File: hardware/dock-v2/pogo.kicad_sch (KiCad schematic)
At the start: 0 parts

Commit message: Dock v2: all parts placed on their sheets (not wired)
149 parts across POWER, USB_PORTS, MCU_A, MCU_B, BLE and POGO (A3), in
labelled groups, with references (sheet x 100), values, footprints, LCSC
numbers (hidden LCSC field) and a Note per part. Only unconnected-pin ERC
messages remain.

5 V buck values from TI's TPS54331 Table 7-1 (5 V design), moved to Basic
parts: 12k/2.2k feedback (5.16 V), 51k + 4.7nF + 47pF compensation, 10 nF
soft start, 3 x 22 uF out; recorded in docs/dock-v2-power-input.md.
New footprint dock_v2:CP_Radial_D6.3mm_P5.00mm for the hand-soldered 220 uF.

Co-Authored-By: Claude Opus 5.5 <noreply@anthropic.com>
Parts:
- added C601, C603: 1uF, Capacitor_SMD:C_0402_1005Metric, symbol Device:C
- added C602: 10uF, Capacitor_SMD:C_0805_2012Metric, symbol Device:C
- added J601: Pogo 6-pin, dock:Pogo-6, symbol Connector_Generic:Conn_01x06
- added Q601: 2N7002, Package_TO_SOT_SMD:SOT-23, symbol Transistor_FET:2N7002
- added R601, R602, R603: 1k, Resistor_SMD:R_0402_1005Metric, symbol Device:R
- added R604, R607: 10k, Resistor_SMD:R_0402_1005Metric, symbol Device:R
- added R605: 100k, Resistor_SMD:R_0402_1005Metric, symbol Device:R
- added R606: 6.8k, Resistor_SMD:R_0402_1005Metric, symbol Device:R
- added R608: 15k, Resistor_SMD:R_0402_1005Metric, symbol Device:R
- added U601: TPD4E1U06DBVR, Package_TO_SOT_SMD:SOT-23-6, symbol dock_v2_custom:TPD4E1U06DBV
- added U602: SY6280AAC, Package_TO_SOT_SMD:SOT-23-5, symbol dock_v2_custom:SY6280AAC
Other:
- note added: "Pogo 5 V switch (hardware DET enable)"
- note added: "Pogo connector (front edge)"

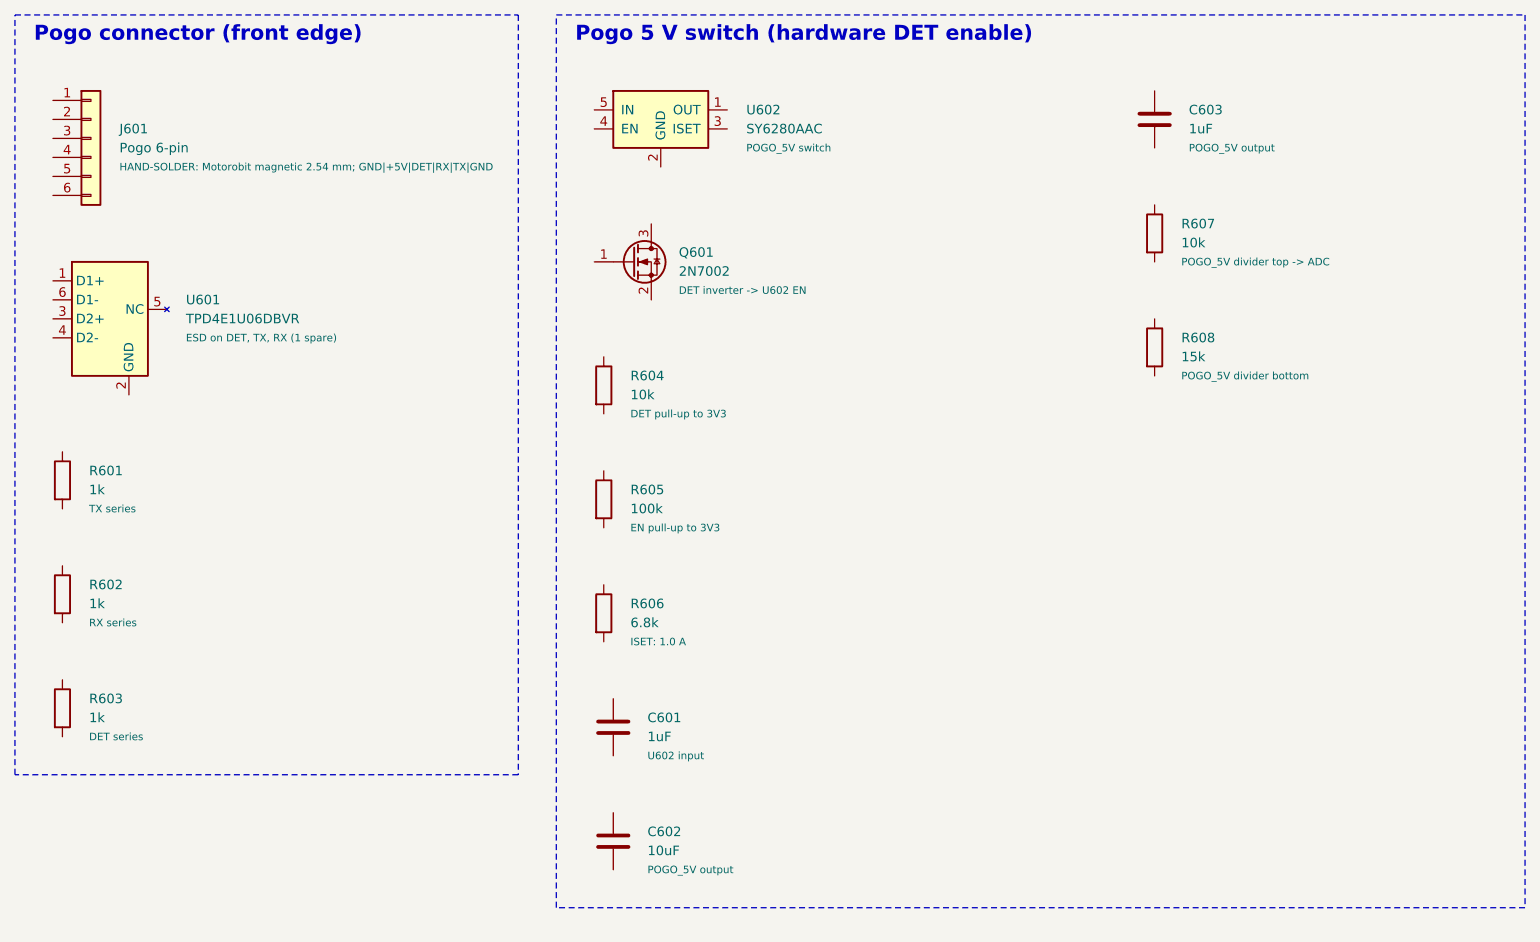
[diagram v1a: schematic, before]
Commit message: Dock v2: connection guide (DOCK_CONNECTIONS.md), pin maps, wiring checker
hardware/dock-v2/DOCK_CONNECTIONS.md, in the style of the pad's guide: per
sheet a sketch, parts table (value, footprint, LCSC, job), pin-by-pin wiring
tables, placement notes; MCU A/B pin maps; nets that cross sheets (global
labels); PWR_FLAG and no-connect lists; full net index. Tables are generated
from one connection model (tools/dock_v2_connections/dock_nets.py) that is
checked against the placed schematic: 570 pins, each on a net or NC exactly once.

Found while making the pin map: MCU A's pins are weak pull-downs at reset, so
added 10k pull-ups on B_RUN, B_BOOTSEL (R406, R407) and ESP32 GPIO9 (R504),
and POGO_OFF now drives its own 2N7002 (Q602, R609) so a blank MCU A can't
switch off pad charging. 154 parts.

tools/dock_v2_connections/check_wiring.py compares the wired schematic with
the guide (unwired / split / merged / NC); make_doc.py regenerates the guide.

Co-Authored-By: Claude Opus 5.5 <noreply@anthropic.com>
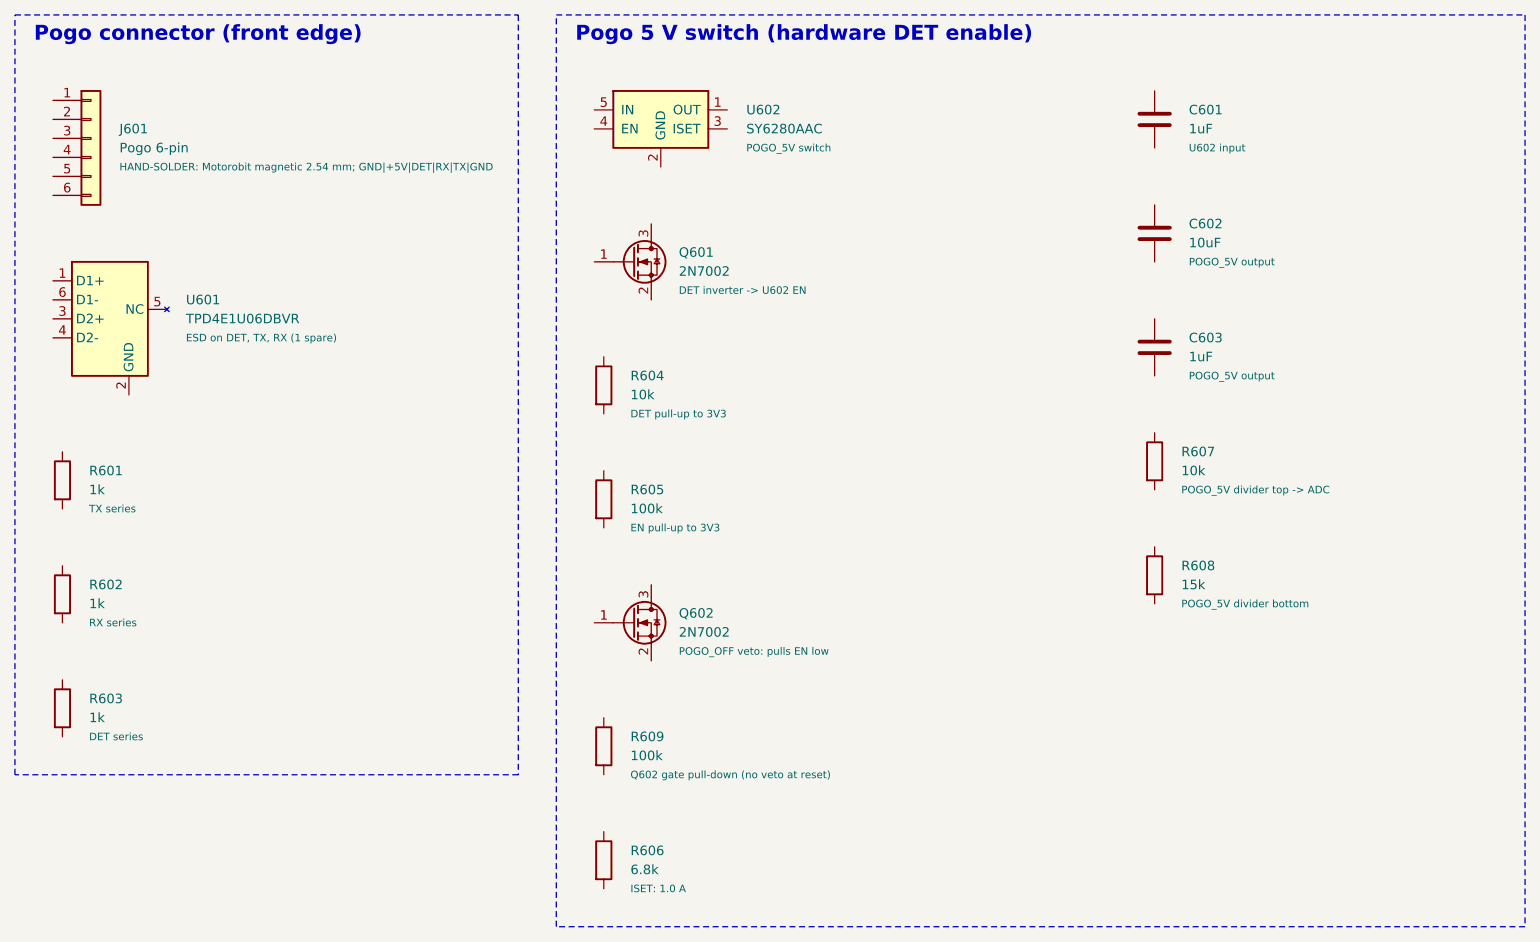
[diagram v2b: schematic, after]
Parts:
- added Q602: 2N7002, Package_TO_SOT_SMD:SOT-23, symbol Transistor_FET:2N7002
- added R609: 100k, Resistor_SMD:R_0402_1005Metric, symbol Device:R

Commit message: 7-pin pogo (2 x +5V, 2 x GND), README and DESIGN for the v2 dock
Pogo: both halves move from the 6-pin to the Motorobit 7-pin 2.54 mm magnetic
set (1 A per contact). Dock side GND | +5V | +5V | DET | RX | TX | GND, pad side
mirrored. New footprint dock:Pogo-7 (scaled from Pogo-6, marked through-hole).
Dock J601 -> Conn_01x07; pogo switch R606 6.8k -> 4.7k (1.45 A, 1.09-1.81 A,
below the 2 A of two contacts), so the pad no longer has to dim its LEDs while
docked. Pad pogo board J1 -> 7 pins, pins 5+6 = POGO_5V, pin 7 = GND (nets
verified before/after). Connection model, guide, pogo/power/placement docs and
PAD_CONNECTIONS updated.

README and DESIGN rewritten for the v2 dock (sections 1-7, 15-22); the pad
sections 8-14 are kept as the v1 plan, to be redesigned. v1 dock stays on master.

Co-Authored-By: Claude Opus 5.5 <noreply@anthropic.com>
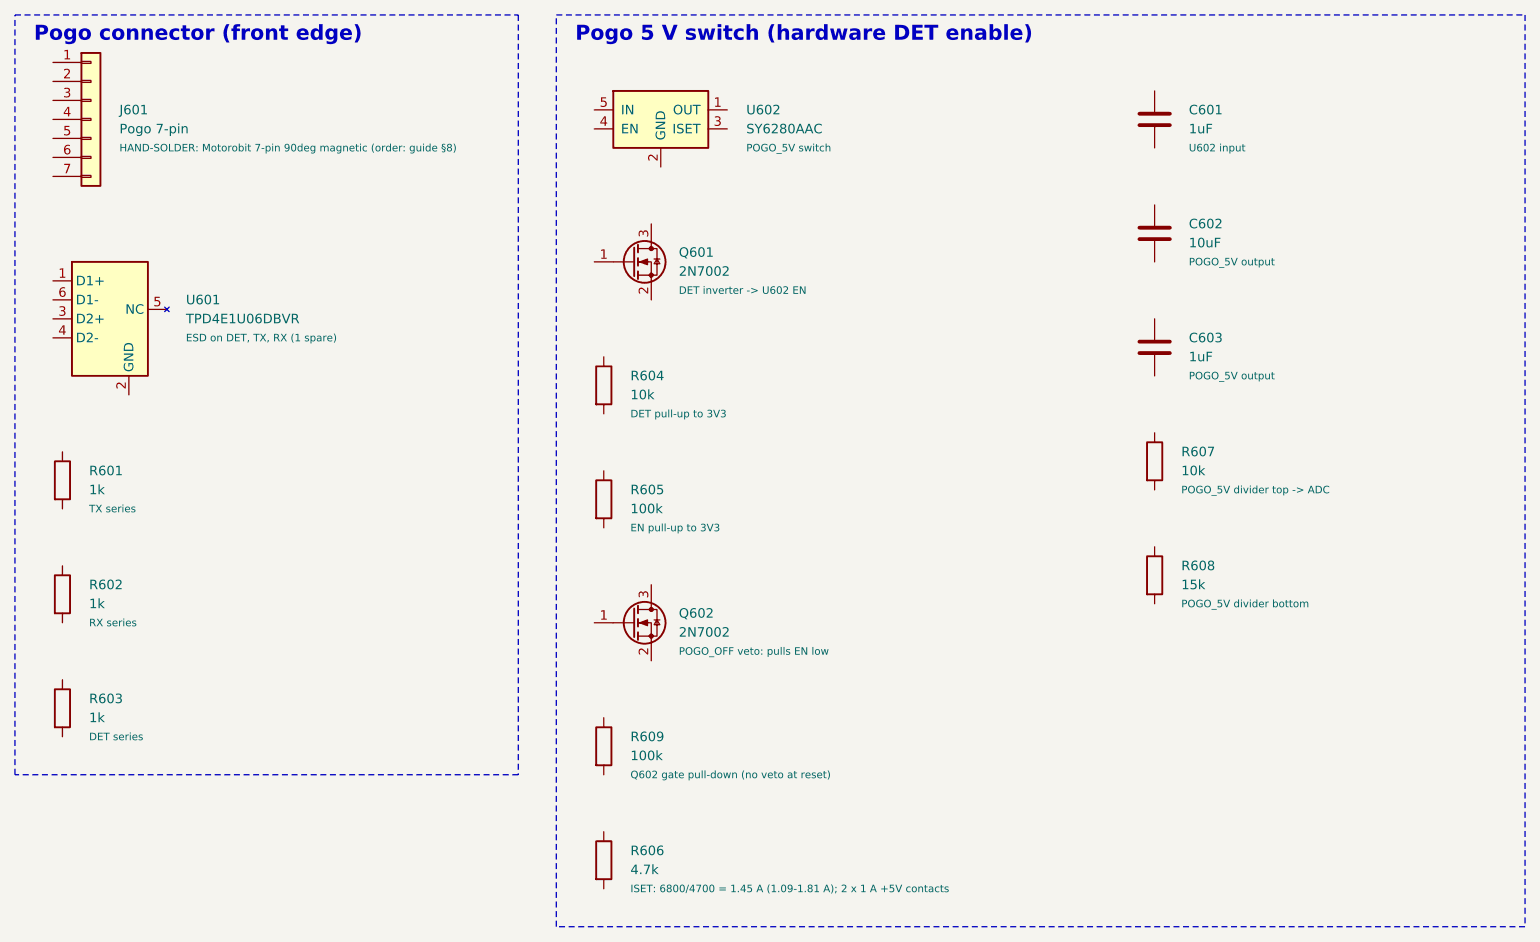
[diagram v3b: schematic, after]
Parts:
- J601: value Pogo 6-pin -> Pogo 7-pin; footprint dock:Pogo-6 -> dock:Pogo-7; symbol Connector_Generic:Conn_01x06 -> Connector_Generic:Conn_01x07; Note HAND-SOLDER: Motorobit magnetic 2.54 mm; GND|+5V|DET|RX|TX|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 -> HAND-SOLDER: Motorobit 7-pin 90deg magnetic (order: guide §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
- R606: value 6.8k -> 4.7k; LCSC C25917 -> C25900; Note ISET: 1.0 A -> ISET: 6800/4700 = 1.45 A (1.09-1.81 A); 2 x 1 A +5V contacts
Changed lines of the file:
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@@
 	)
 	(symbol
-		(lib_id "Connector_Generic:Conn_01x06")
-		(at 22.86 34.29 0)
+		(lib_id "Connector_Generic:Conn_01x07")
+		(at 22.86 31.75 0)
 		(unit 1)
 		(body_style 1)
@@
 		(fields_autoplaced no)
 		(property "Reference" "J601"
+			(at 26.67 30.48 0)
+			(show_name no)
+			(do_not_autoplace no)
+			(effects
+				(font
+					(size 1.27 1.27)
+				)
+				(justify left)
+			)
+		)
+		(property "Value" "Pogo 7-pin"
 			(at 26.67 33.02 0)
 			(show_name no)
@@
 			)
 		)
-		(property "Value" "Pogo 6-pin"
+		(property "Footprint" "dock:Pogo-7"
+			(at 22.86 31.75 0)
+			(hide yes)
+			(show_name no)
+			(do_not_autoplace no)
+			(effects
+				(font
+					(size 1.27 1.27)
+				)
+			)
+		)
+		(property "Datasheet" ""
+			(at 22.86 31.75 0)
+			(hide yes)
+			(show_name no)
+			(do_not_autoplace no)
+			(effects
+				(font
+					(size 1.27 1.27)
+				)
+			)
+		)
+		(property "Description" "Generic connector, single row, 01x06, script generated (kicad-library-utils/schlib/autogen/connector/)"
+			(at 22.86 31.75 0)
+			(hide yes)
+			(show_name no)
+			(do_not_autoplace no)
+			(effects
+				(font
+					(size 1.27 1.27)
+				)
+			)
+		)
+		(property "LCSC" ""
+			(at 22.86 31.75 0)
+			(hide yes)
+			(show_name no)
+			(do_not_autoplace no)
+			(effects
+				(font
+					(size 1.27 1.27)
+				)
+			)
+		)
+		(property "Note" "HAND-SOLDER: Motorobit 7-pin 90deg magnetic (order: guide §8)"
 			(at 26.67 35.56 0)
 			(show_name no)
@@
 			(effects
 				(font
-					(size 1.27 1.27)
-				)
-				(justify left)
-			)
-		)
-		(property "Footprint" "dock:Pogo-6"
-			(at 22.86 34.29 0)
-			(hide yes)
-			(show_name no)
-			(do_not_autoplace no)
-			(effects
-				(font
-					(size 1.27 1.27)
-				)
-			)
-		)
-		(property "Datasheet" ""
-			(at 22.86 34.29 0)
-			(hide yes)
-			(show_name no)
-			(do_not_autoplace no)
-			(effects
-				(font
-					(size 1.27 1.27)
-				)
-			)
-		)
-		(property "Description" "Generic connector, single row, 01x06, script generated (kicad-library-utils/schlib/autogen/connector/)"
-			(at 22.86 34.29 0)
-			(hide yes)
-			(show_name no)
-			(do_not_autoplace no)
-			(effects
-				(font
-					(size 1.27 1.27)
-				)
-			)
-		)
-		(property "LCSC" ""
-			(at 22.86 34.29 0)
-			(hide yes)
-			(show_name no)
-			(do_not_autoplace no)
-			(effects
-				(font
-					(size 1.27 1.27)
-				)
-			)
-		)
-		(property "Note" "HAND-SOLDER: Motorobit magnetic 2.54 mm; GND|+5V|DET|RX|TX|GND"
-			(at 26.67 38.10 0)
-			(show_name no)
-			(do_not_autoplace no)
-			(effects
-				(font
 					(size 1.0 1.0)
 				)
@@
 		)
 		(pin "6"
+		)
+		(pin "7"
 		)
 		(instances
@@
 			)
 		)
-		(property "Value" "6.8k"
+		(property "Value" "4.7k"
 			(at 95.00 132.08 0)
 			(show_name no)
@@
 			)
 		)
-		(property "LCSC" "C25917"
+		(property "LCSC" "C25900"
 			(at 91.44 130.81 0)
 			(hide yes)
@@
 			)
 		)
-		(property "Note" "ISET: 1.0 A"
+		(property "Note" "ISET: 6800/4700 = 1.45 A (1.09-1.81 A); 2 x 1 A +5V contacts"
 			(at 95.00 134.62 0)
 			(show_name no)
